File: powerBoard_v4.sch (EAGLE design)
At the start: 25 parts, among them U1 TLE2426CD

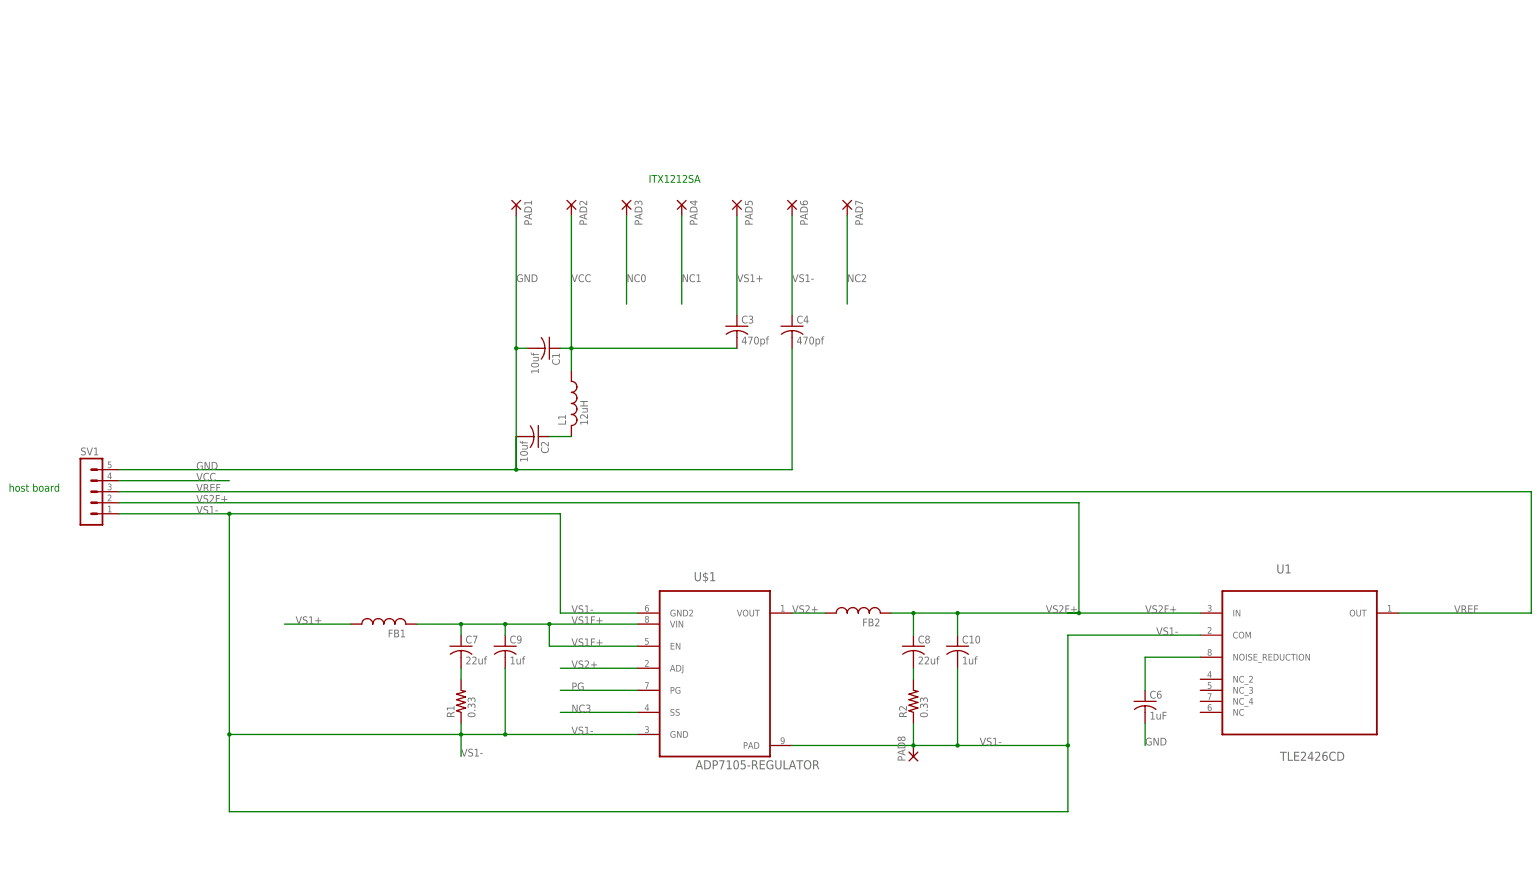
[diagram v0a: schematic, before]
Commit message: updated power board designs: v2 uses low current 2.5v reference, v3 uses 10v rail and 5v ref both with simple linear regulators. Added breakout board to go from DB37 to BNC
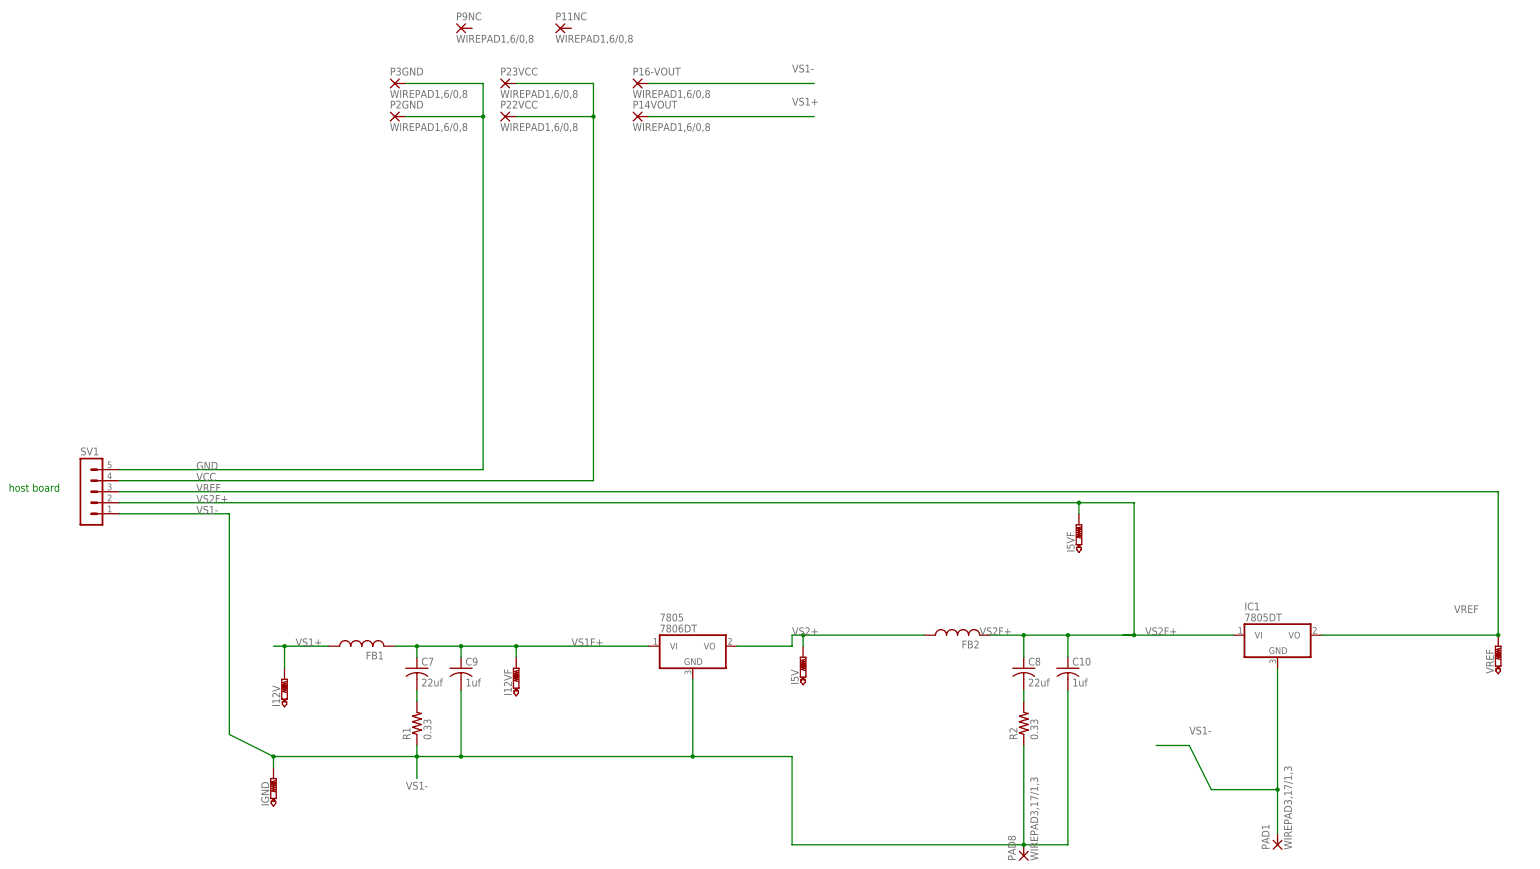
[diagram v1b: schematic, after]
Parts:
- removed C1, C2: 10uf, rcl:C-USC0805K
- removed C3, C4: 470pf, rcl:C-USC0805K
- removed C6: 1uF, rcl:C-USC0805
- removed L1: 12uH, resistor:L-USL2012C
- removed PAD2, PAD3, PAD4, PAD5, PAD6, PAD7: (no value), wirepad:SMD2
- removed U$1: ADP7105-REGULATOR, tuckerLib:ADP7105-REGULATOR
- removed U1: TLE2426CD, Texas Instruments_By_element14_Batch_1:TLE2426CD
- added 7805: 7806DT, linear:7806DT
- added I12V, I12VF, I5V, I5VF, IGND, VREF: PTR1PAD1-13, testpad:PTR1PAD1-13
- added IC1: 7805DT, linear:7805DT
- added P11NC, P14VOUT, P16-VOUT, P22VCC, P23VCC, P2GND, P3GND, P9NC: WIREPAD1,6/0,8, wirepad:WIREPAD1,6/0,8
- PAD1: value (none) -> WIREPAD3,17/1,3; device wirepad:SMD2 -> wirepad:WIREPAD3,17/1,3
- PAD8: value (none) -> WIREPAD3,17/1,3; device wirepad:2,54/1,1 -> wirepad:WIREPAD3,17/1,3
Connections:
- removed net N$1: C2.1, L1.2
- removed net N$2: C6.1, U1.NOISE_REDUCTION
- removed net NC0: PAD3.P
- removed net NC1: PAD4.P
- removed net NC2: PAD7.P
- removed net NC3: U$1.SS
- removed net PG: U$1.PG
- net GND: now also P2GND.P, P3GND.P; no longer C1.2, C2.2, C4.2, C6.2, PAD1.P
- net VCC: now also P22VCC.P, P23VCC.P; no longer C1.1, C3.2, L1.1, PAD2.P
- net VREF: now also IC1.VO, VREF.TP; no longer U1.OUT
- net VS1+: now also I12V.TP, P14VOUT.P; no longer C3.1, PAD5.P
- net VS1-: now also 7805.GND, IC1.GND, IGND.TP, P16-VOUT.P, PAD1.P; no longer C4.1, PAD6.P, U$1.GND, U$1.GND2, U$1.PAD, U1.COM
- net VS1F+: now also 7805.VI, I12VF.TP; no longer U$1.EN, U$1.VIN
- net VS2+: now also 7805.VO, I5V.TP; no longer U$1.ADJ, U$1.VOUT
- net VS2F+: now also I5VF.TP, IC1.VI; no longer U1.IN
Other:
- note removed: "ITX1212SA"
- moved on the sheet: C10, C7, C8, C9, FB1, FB2, R1, R2

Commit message: updated V4 powerboard to actually include switchmode pads. Added BOM for backplane and daughter card
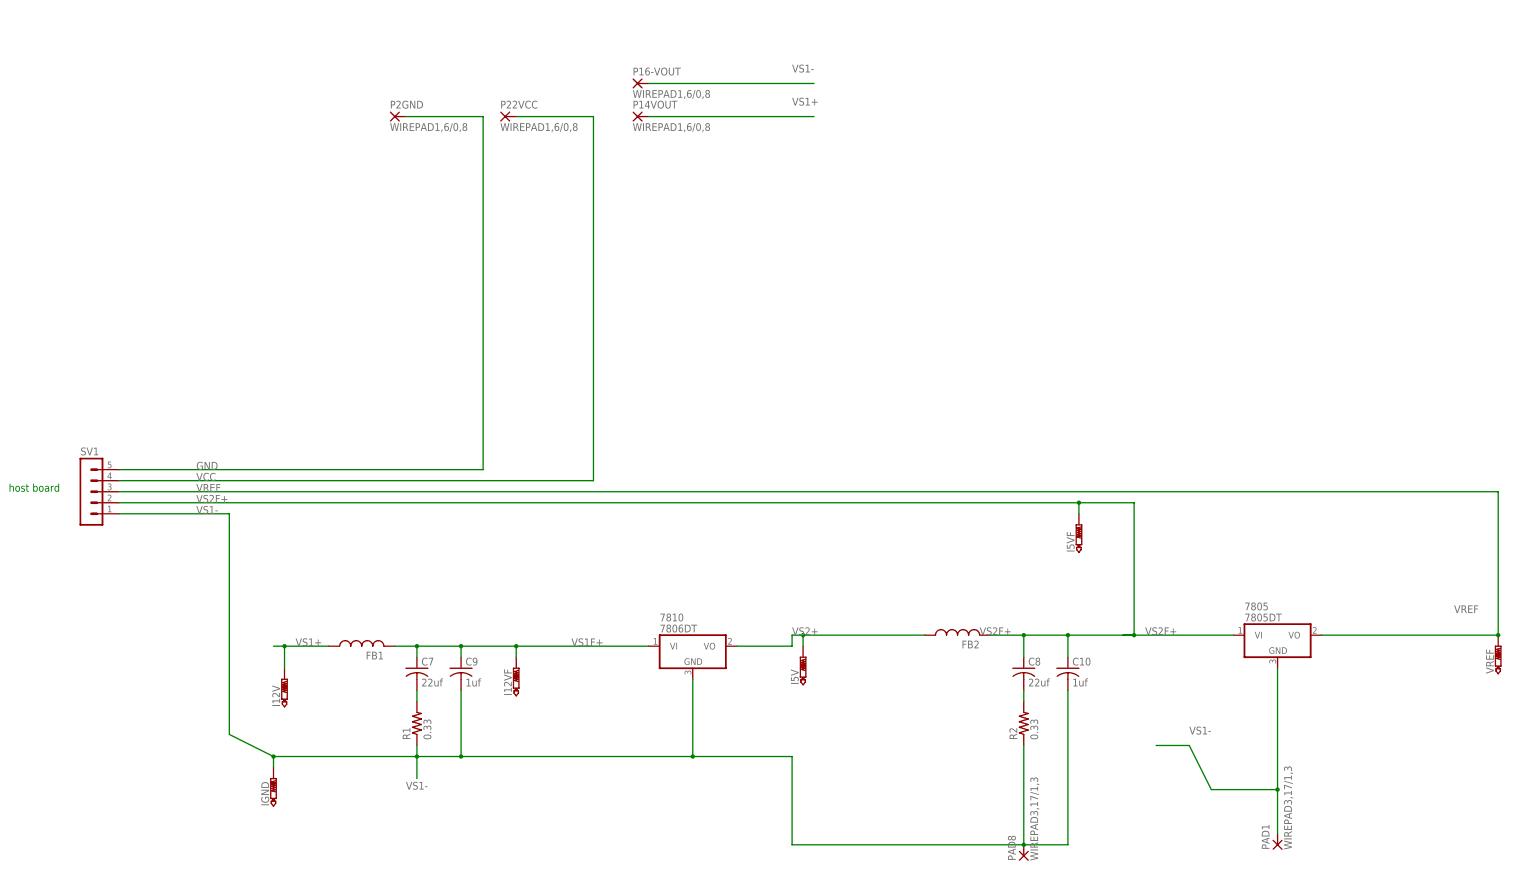
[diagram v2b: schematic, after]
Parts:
- removed IC1: 7805DT, linear:7805DT
- removed P11NC, P23VCC, P3GND, P9NC: WIREPAD1,6/0,8, wirepad:WIREPAD1,6/0,8
- added 7810: 7806DT, linear:7806DT
- 7805: value 7806DT -> 7805DT; device linear:7806DT -> linear:7805DT
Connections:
- net GND: no longer P3GND.P
- net VCC: no longer P23VCC.P
- net VREF: now also 7805.VO; no longer IC1.VO
- net VS1-: now also 7810.GND; no longer IC1.GND
- net VS1F+: now also 7810.VI; no longer 7805.VI
- net VS2+: now also 7810.VO; no longer 7805.VO
- net VS2F+: now also 7805.VI; no longer IC1.VI
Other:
- moved on the sheet: 7805
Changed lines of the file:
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@@
 <part name="IGND" library="testpad" deviceset="PTR1" device="PAD1-13"/>
 <part name="VREF" library="testpad" deviceset="PTR1" device="PAD1-13"/>
-<part name="7805" library="linear" deviceset="78*" device="DT" technology="06"/>
-<part name="IC1" library="linear" deviceset="78*" device="DT" technology="05"/>
+<part name="7810" library="linear" deviceset="78*" device="DT" technology="06"/>
+<part name="7805" library="linear" deviceset="78*" device="DT" technology="05"/>
 <part name="P2GND" library="wirepad" deviceset="WIREPAD" device="1,6/0,8"/>
-<part name="P3GND" library="wirepad" deviceset="WIREPAD" device="1,6/0,8"/>
-<part name="P9NC" library="wirepad" deviceset="WIREPAD" device="1,6/0,8"/>
-<part name="P11NC" library="wirepad" deviceset="WIREPAD" device="1,6/0,8"/>
-<part name="P23VCC" library="wirepad" deviceset="WIREPAD" device="1,6/0,8"/>
 <part name="P22VCC" library="wirepad" deviceset="WIREPAD" device="1,6/0,8"/>
 <part name="P16-VOUT" library="wirepad" deviceset="WIREPAD" device="1,6/0,8"/>
@@
 <instance part="IGND" gate="G$1" x="7.62" y="-10.16"/>
 <instance part="VREF" gate="G$1" x="289.56" y="20.32"/>
-<instance part="7805" gate="A1" x="104.14" y="20.32"/>
-<instance part="IC1" gate="A1" x="238.76" y="22.86"/>
+<instance part="7810" gate="A1" x="104.14" y="20.32"/>
+<instance part="7805" gate="A1" x="238.76" y="22.86"/>
 <instance part="P2GND" gate="G$1" x="35.56" y="142.24"/>
-<instance part="P3GND" gate="G$1" x="35.56" y="149.86"/>
-<instance part="P9NC" gate="G$1" x="50.8" y="162.56"/>
-<instance part="P11NC" gate="G$1" x="73.66" y="162.56"/>
-<instance part="P23VCC" gate="G$1" x="60.96" y="149.86"/>
 <instance part="P22VCC" gate="G$1" x="60.96" y="142.24"/>
 <instance part="P16-VOUT" gate="G$1" x="91.44" y="149.86"/>
@@
 <label x="-10.16" y="60.96" size="1.778" layer="95"/>
 <wire x1="-27.94" y1="60.96" x2="55.88" y2="60.96" width="0.1524" layer="91"/>
-<pinref part="P3GND" gate="G$1" pin="P"/>
-<wire x1="38.1" y1="149.86" x2="55.88" y2="149.86" width="0.1524" layer="91"/>
-<wire x1="55.88" y1="149.86" x2="55.88" y2="142.24" width="0.1524" layer="91"/>
 <pinref part="P2GND" gate="G$1" pin="P"/>
 <wire x1="55.88" y1="142.24" x2="38.1" y2="142.24" width="0.1524" layer="91"/>
 <wire x1="55.88" y1="142.24" x2="55.88" y2="60.96" width="0.1524" layer="91"/>
-<junction x="55.88" y="142.24"/>
 </segment>
 </net>
@@
 <pinref part="P22VCC" gate="G$1" pin="P"/>
 <wire x1="81.28" y1="142.24" x2="63.5" y2="142.24" width="0.1524" layer="91"/>
-<pinref part="P23VCC" gate="G$1" pin="P"/>
-<wire x1="63.5" y1="149.86" x2="81.28" y2="149.86" width="0.1524" layer="91"/>
-<wire x1="81.28" y1="149.86" x2="81.28" y2="142.24" width="0.1524" layer="91"/>
-<junction x="81.28" y="142.24"/>
 </segment>
 </net>
@@
 <pinref part="VREF" gate="G$1" pin="TP"/>
 <junction x="289.56" y="22.86"/>
-<pinref part="IC1" gate="A1" pin="VO"/>
+<pinref part="7805" gate="A1" pin="VO"/>
 </segment>
 </net>
@@
 <wire x1="129.54" y1="20.32" x2="129.54" y2="22.86" width="0.1524" layer="91"/>
 <junction x="129.54" y="22.86"/>
-<pinref part="7805" gate="A1" pin="VO"/>
+<pinref part="7810" gate="A1" pin="VO"/>
 <wire x1="114.3" y1="20.32" x2="127" y2="20.32" width="0.1524" layer="91"/>
 <wire x1="127" y1="20.32" x2="127" y2="22.86" width="0.1524" layer="91"/>
@@
 <wire x1="7.62" y1="-7.62" x2="7.62" y2="-5.08" width="0.1524" layer="91"/>
 <junction x="7.62" y="-5.08"/>
-<pinref part="7805" gate="A1" pin="GND"/>
+<pinref part="7810" gate="A1" pin="GND"/>
 <wire x1="50.8" y1="-5.08" x2="104.14" y2="-5.08" width="0.1524" layer="91"/>
 <wire x1="104.14" y1="-5.08" x2="104.14" y2="12.7" width="0.1524" layer="91"/>
@@
 <wire x1="210.82" y1="-2.54" x2="218.44" y2="-2.54" width="0.1524" layer="91"/>
 <label x="218.44" y="0" size="1.778" layer="95"/>
-<pinref part="IC1" gate="A1" pin="GND"/>
+<pinref part="7805" gate="A1" pin="GND"/>
 <wire x1="238.76" y1="15.24" x2="238.76" y2="-12.7" width="0.1524" layer="91"/>
 <wire x1="238.76" y1="-12.7" x2="223.52" y2="-12.7" width="0.1524" layer="91"/>
@@
 <wire x1="193.04" y1="50.8" x2="193.04" y2="53.34" width="0.1524" layer="91"/>
 <junction x="193.04" y="53.34"/>
-<pinref part="IC1" gate="A1" pin="VI"/>
+<pinref part="7805" gate="A1" pin="VI"/>
 </segment>
 </net>
@@
 <wire x1="63.5" y1="17.78" x2="63.5" y2="20.32" width="0.1524" layer="91"/>
 <junction x="63.5" y="20.32"/>
-<pinref part="7805" gate="A1" pin="VI"/>
-</segment>
-</net>
+<pinref part="7810" gate="A1" pin="VI"/>
+</segment>
+</net>

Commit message: minor labeling and component placement updates. most significant is correcting part position on powerboard so 22uF bypass cap actually connects to ground.
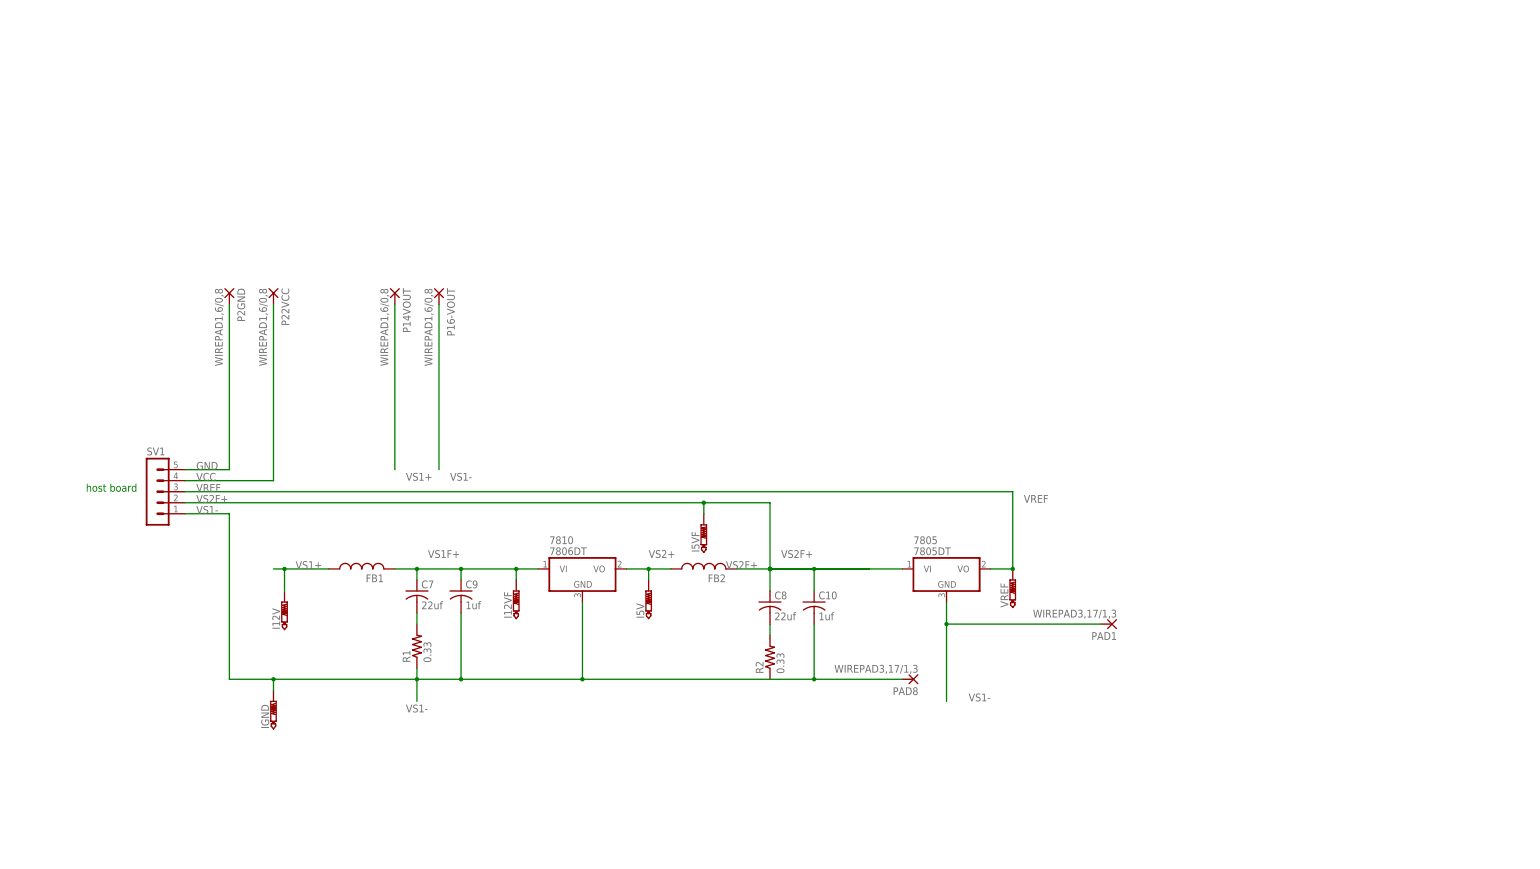
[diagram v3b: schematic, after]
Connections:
- net VS1-: no longer R2.1
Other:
- moved on the sheet: 7805, 7810, C10, C7, C8, C9, FB1, FB2, I12V, I12VF, I5V, I5VF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
